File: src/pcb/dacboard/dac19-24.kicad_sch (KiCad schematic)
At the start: 18 parts, among them U46 AD8676xR, U47 AD8676xR, U48 AD8676xR, U49 AD8676xR, U50 AD5791BRUZ, U51 AD5791BRUZ, U52 AD5791BRUZ, U53 AD5791BRUZ, U54 AD8676xR, U55 AD8676xR, U56 AD5791BRUZ, U57 AD5791BRUZ

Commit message: dacboard routing
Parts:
- C40, C41, C42, C43, C44, C45: value C -> 10uF; footprint (none) -> Capacitor_SMD:C_0603_1608Metric_Pad1.08x0.95mm_HandSolder
- U50, U51, U52, U53, U56, U57: footprint RU_20_ADI -> Package_SO:TSSOP-20_4.4x6.5mm_P0.65mm

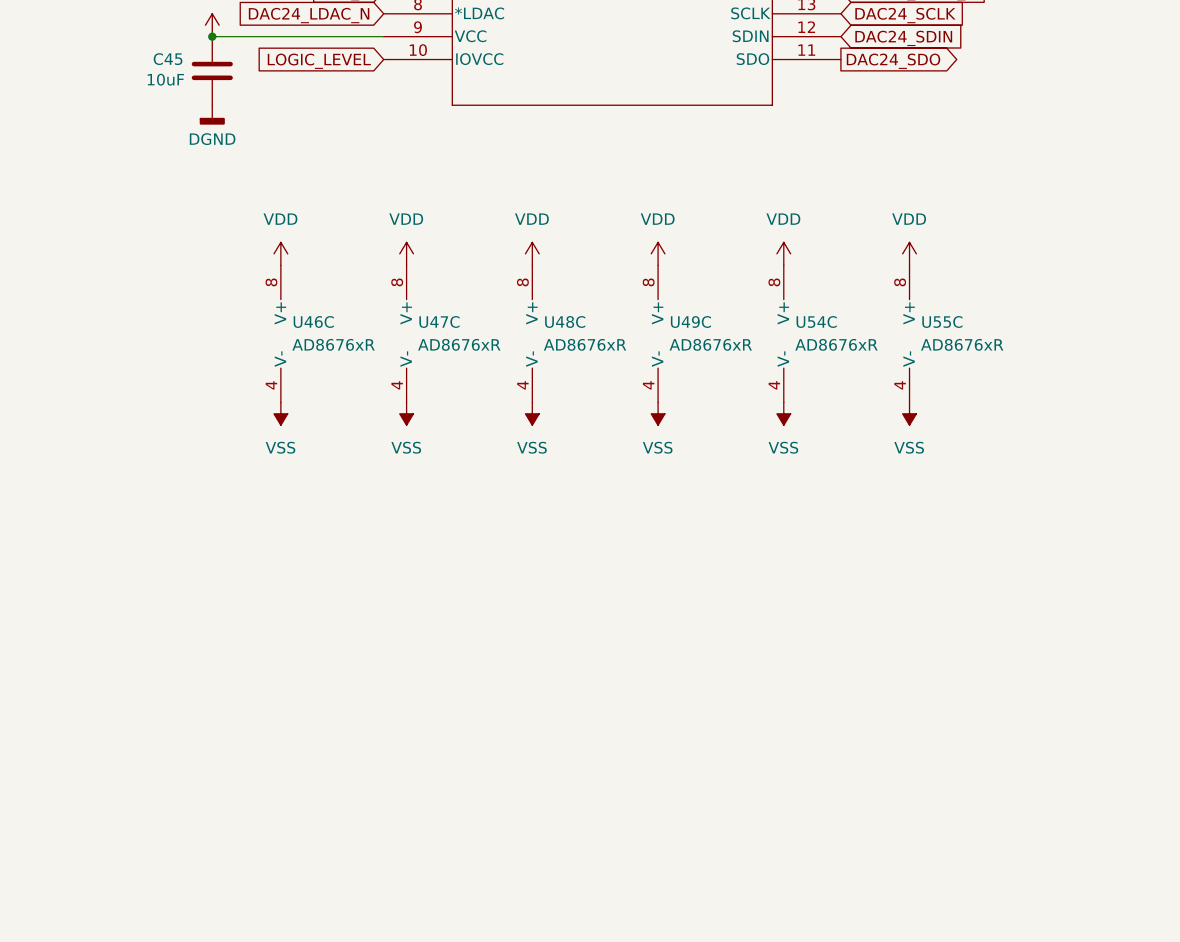
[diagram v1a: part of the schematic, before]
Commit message: adding more capacitors to analog side
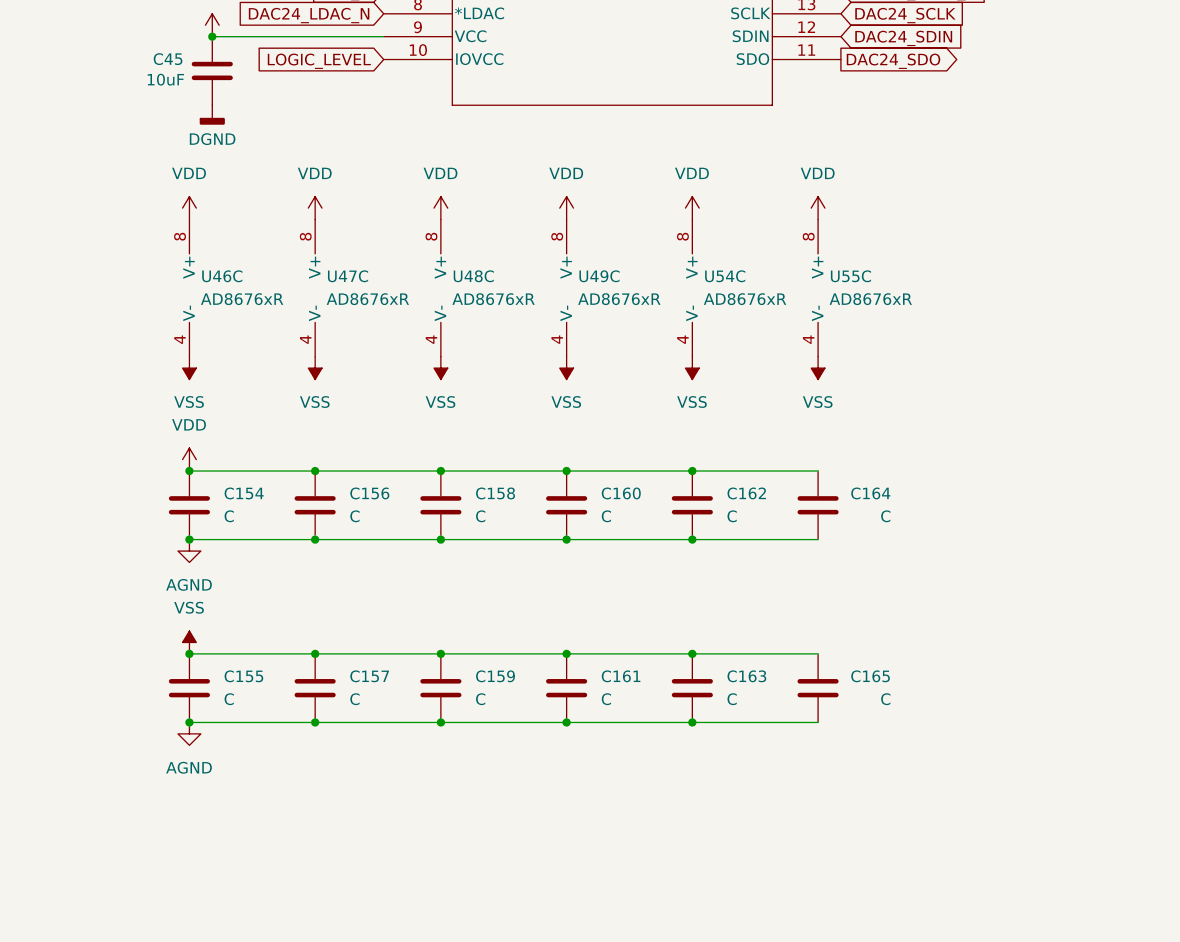
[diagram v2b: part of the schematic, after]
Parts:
- added C154, C155, C156, C157, C158, C159, C160, C161, C162, C163, C164, C165: C, Capacitor_SMD:C_0402_1005Metric_Pad0.74x0.62mm_HandSolder, symbol Device:C
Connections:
- net AGND: now also C154.2, C155.2, C156.2, C157.2, C158.2, C159.2, C160.2, C161.2, C162.2, C163.2, C164.2, C165.2
- net VDD: now also C154.1, C156.1, C158.1, C160.1, C162.1, C164.1
- net VSS: now also C155.1, C157.1, C159.1, C161.1, C163.1, C165.1
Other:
- moved on the sheet: U46C, U47C, U48C, U49C, U54C, U55C

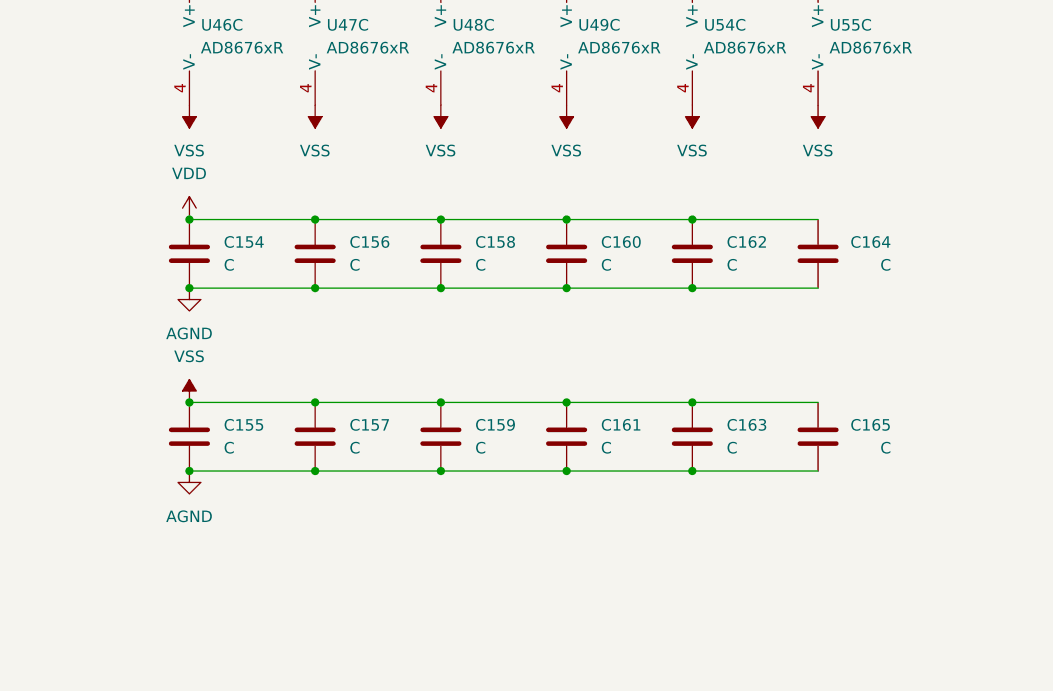
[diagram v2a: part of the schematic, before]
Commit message: more capacitors
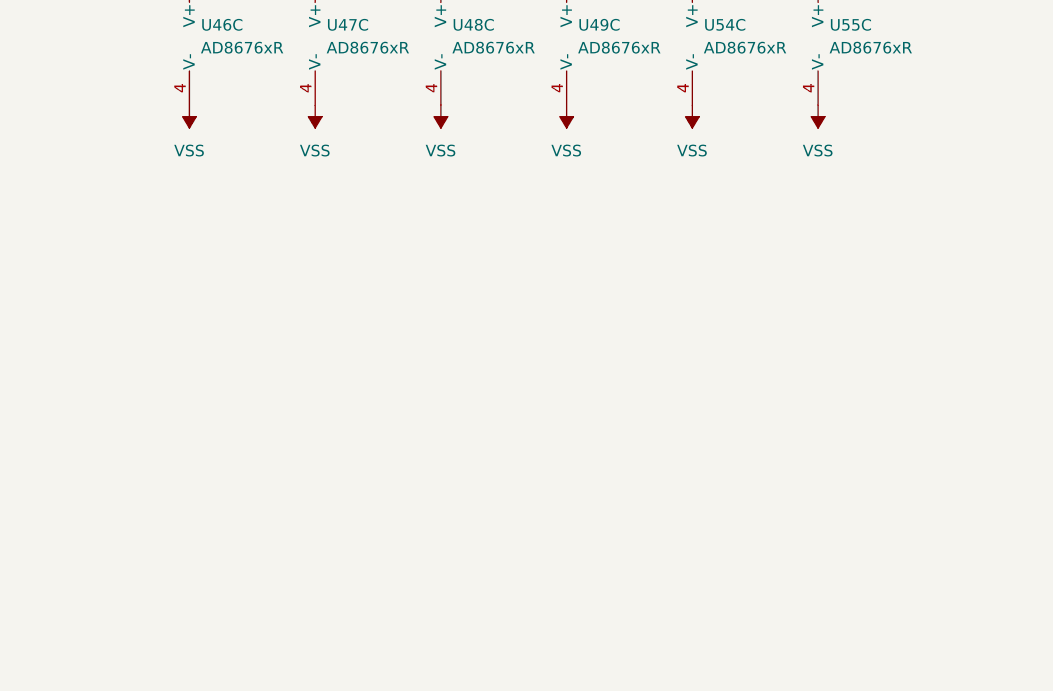
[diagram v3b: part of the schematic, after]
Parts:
- removed C154, C155, C156, C157, C158, C159, C160, C161, C162, C163, C164, C165: C, Capacitor_SMD:C_0402_1005Metric_Pad0.74x0.62mm_HandSolder, symbol Device:C

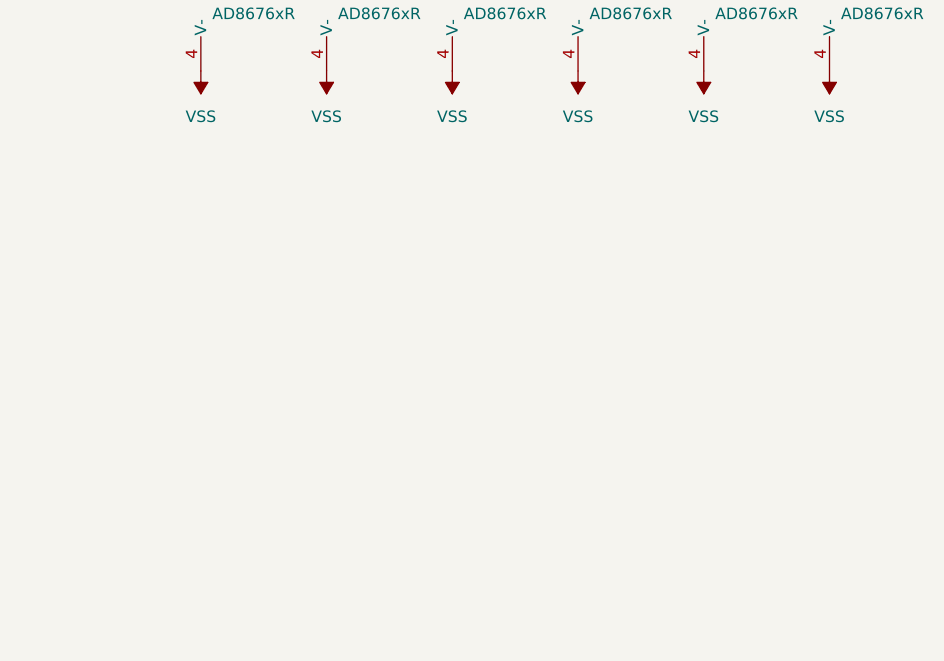
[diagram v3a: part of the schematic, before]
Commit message: got rid of all drc errors
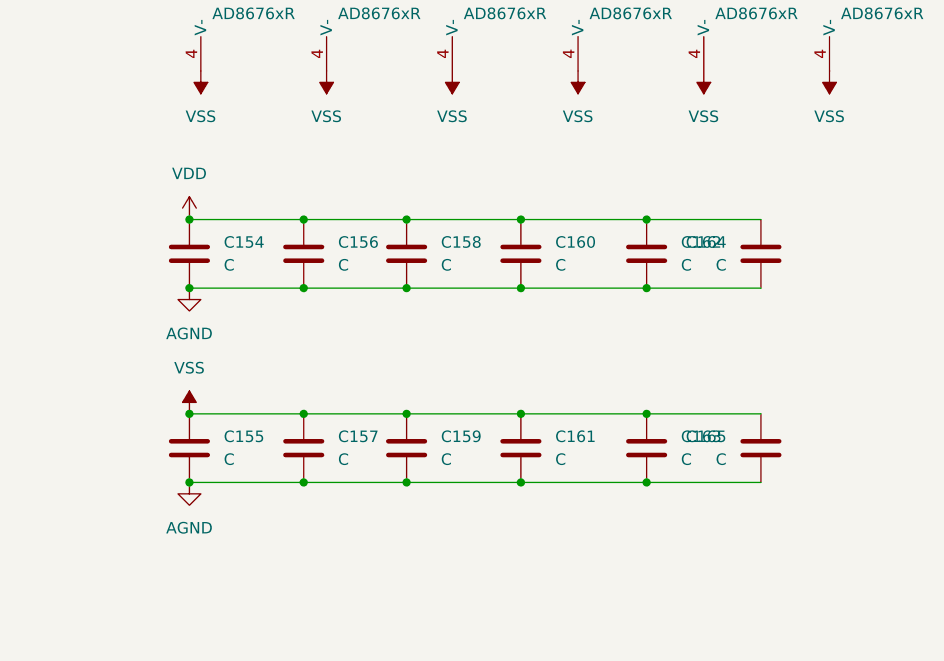
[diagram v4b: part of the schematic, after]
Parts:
- added C154, C155, C156, C157, C158, C159, C160, C161, C162, C163, C164, C165: C, Capacitor_SMD:C_0402_1005Metric_Pad0.74x0.62mm_HandSolder, symbol Device:C
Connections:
- net AGND: now also C154.2, C155.2, C156.2, C157.2, C158.2, C159.2, C160.2, C161.2, C162.2, C163.2, C164.2, C165.2
- net VDD: now also C154.1, C156.1, C158.1, C160.1, C162.1, C164.1
- net VSS: now also C155.1, C157.1, C159.1, C161.1, C163.1, C165.1
